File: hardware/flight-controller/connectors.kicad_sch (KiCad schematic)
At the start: 44 parts, among them J10 Conn_01x03, J11 IDC-10, J3 Conn_01x03, J4 IDC-10, J5 Conn_01x03, J6 Conn_01x03, J7 IDC-10, J8 Conn_01x03, J9 XT-30

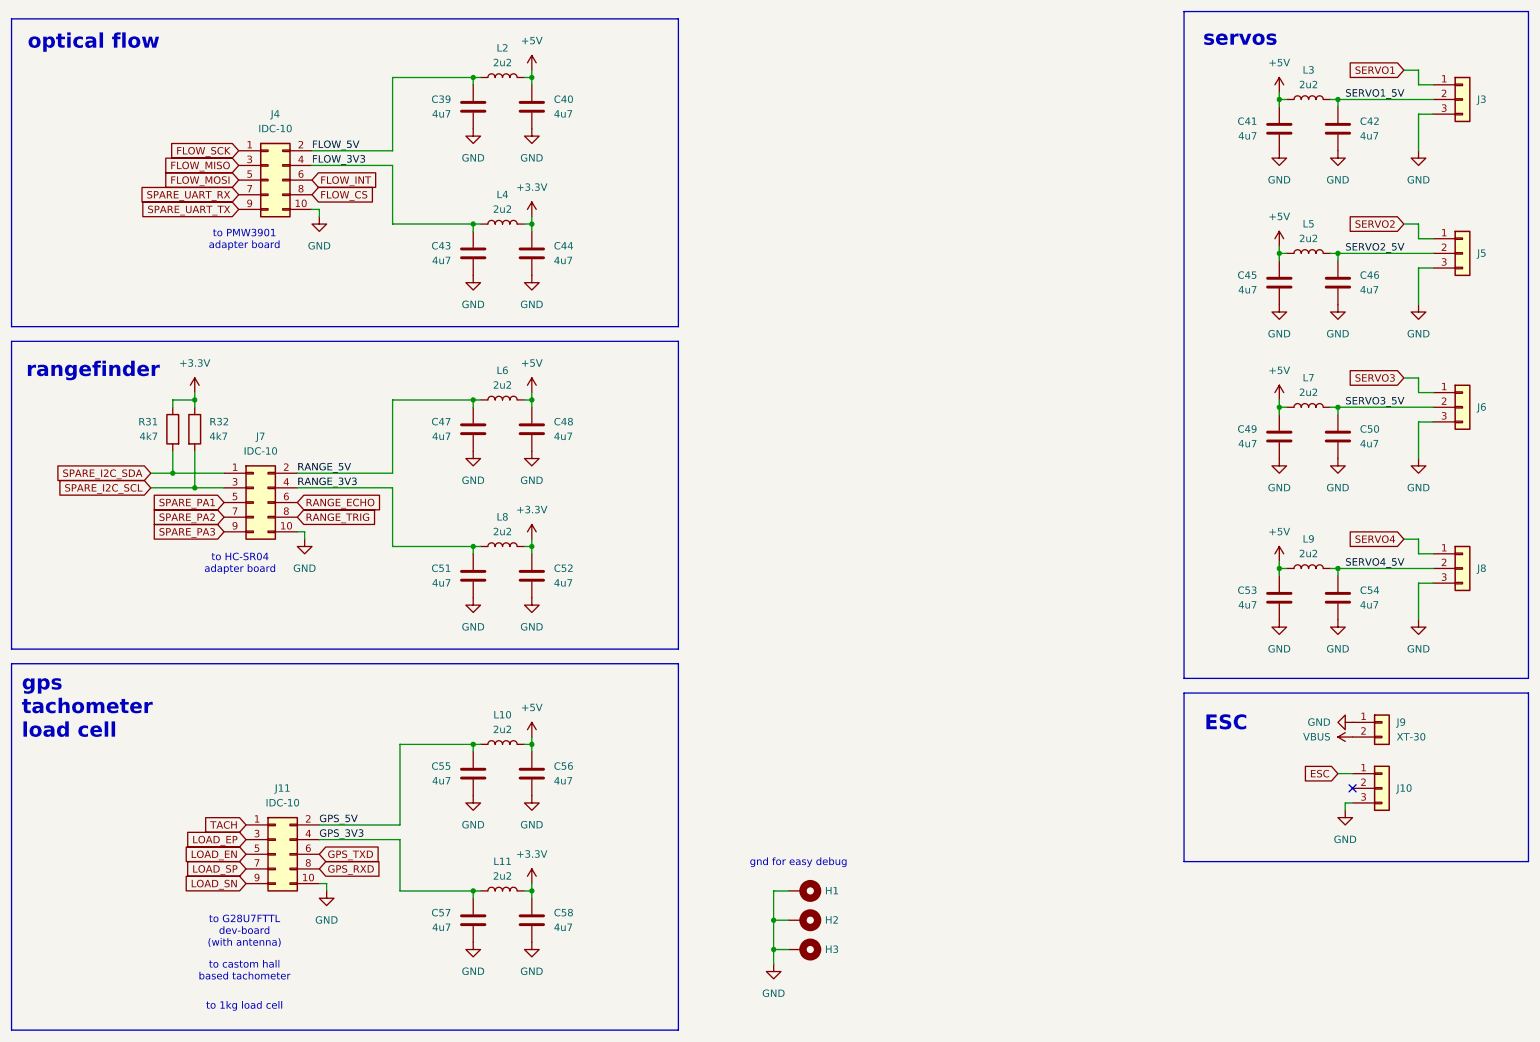
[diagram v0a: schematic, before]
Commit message: clean footprints
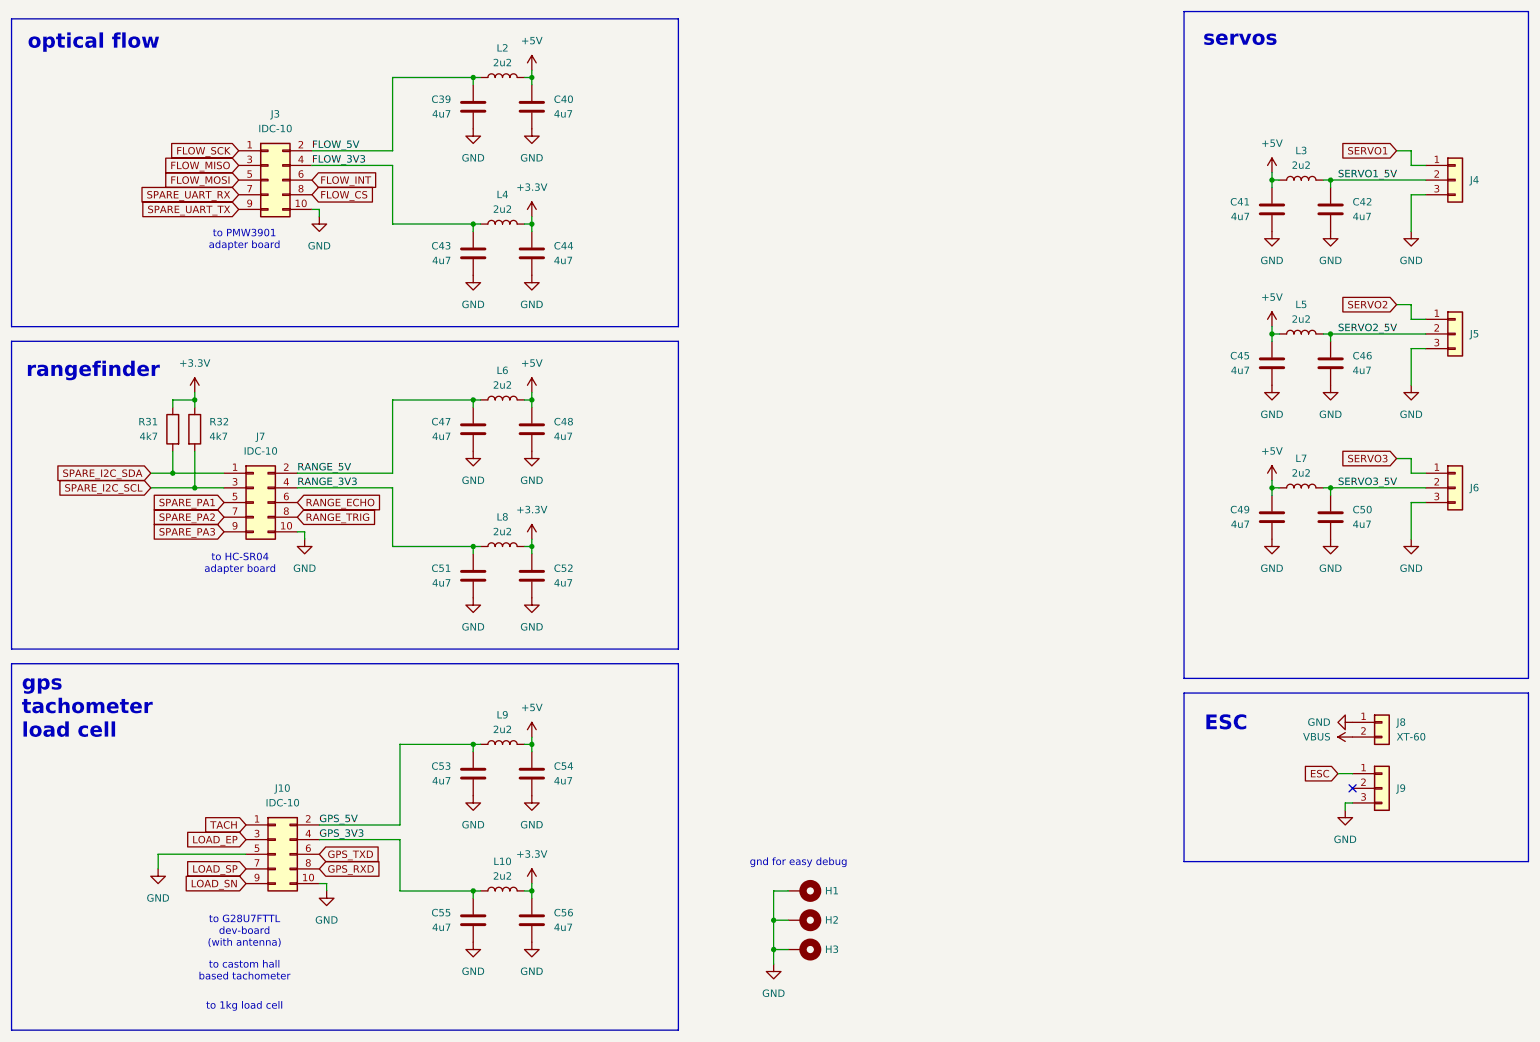
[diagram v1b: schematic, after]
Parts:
- removed C53, C54: 4u7, symbol Device:C
- removed J8: Conn_01x03, Connector_PinHeader_2.54mm:PinHeader_1x03_P2.54mm_Vertical, symbol Connector_Generic:Conn_01x03
- removed L9: 2u2, symbol Device:L
- J10: renamed from J11; footprint Connector_IDC:IDC-Header_2x05_P2.54mm_Horizontal -> goose:IDC-10-horizontal
- J3: renamed from J4; footprint Connector_IDC:IDC-Header_2x05_P2.54mm_Horizontal -> goose:IDC-10-horizontal
- J4: renamed from J3; footprint Connector_PinHeader_2.54mm:PinHeader_1x03_P2.54mm_Vertical -> goose:header_1x3
- J5, J6: footprint Connector_PinHeader_2.54mm:PinHeader_1x03_P2.54mm_Vertical -> goose:header_1x3
- J7: footprint Connector_IDC:IDC-Header_2x05_P2.54mm_Horizontal -> goose:IDC-10-horizontal
- J8: renamed from J9; value XT-30 -> XT-60; footprint Connector_AMASS:AMASS_XT30PW-F_1x02_P2.50mm_Horizontal -> goose:XT60PW-F
- J9: renamed from J10; footprint Connector_PinHeader_2.54mm:PinHeader_1x03_P2.54mm_Vertical -> goose:header_1x3
- renumbered C55 to C53, C56 to C54, C57 to C55, C58 to C56, L11 to L10, L10 to L9
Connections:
- net LOAD_EN is gone; now on net GND: J10.5 (Pin_5)
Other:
- moved on the sheet: C41, C42, C45, C46, C49, C50, J4, J5, J6, L3, L5, L7

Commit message: PI LC filters values
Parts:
- C39, C40, C41, C42, C43, C44, C45, C46, C47, C48, C49, C50, C51, C52, C53, C54, C55, C56: value 4u7 -> 10u; footprint (none) -> Capacitor_SMD:C_0603_1608Metric
- L10, L2, L3, L4, L5, L6, L7, L8, L9: footprint (none) -> Inductor_SMD:L_0603_1608Metric
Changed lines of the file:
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@@
 			)
 		)
-		(property "Footprint" ""
+		(property "Footprint" "Inductor_SMD:L_0603_1608Metric"
 			(at 242.57 97.79 0)
 			(effects
@@
 			)
 		)
-		(property "Value" "4u7"
+		(property "Value" "10u"
 			(at 251.46 50.7999 0)
 			(effects
@@
 			)
 		)
-		(property "Footprint" ""
+		(property "Footprint" "Capacitor_SMD:C_0603_1608Metric"
 			(at 248.6152 53.34 0)
 			(effects
@@
 			)
 		)
-		(property "Footprint" ""
+		(property "Footprint" "Inductor_SMD:L_0603_1608Metric"
 			(at 104.14 52.07 0)
 			(effects
@@
 		(lib_id "Device:C")
 		(at 99.06 147.32 0)
-		(mirror y)
 		(unit 1)
 		(exclude_from_sim no)
@@
 		(on_board yes)
 		(dnp no)
-		(fields_autoplaced yes)
 		(property "Reference" "C53"
 			(at 95.25 146.0499 0)
@@
 					(size 1.27 1.27)
 				)
-				(justify left)
+				(justify right)
 			)
 		)
-		(property "Value" "4u7"
+		(property "Value" "10u"
 			(at 95.25 148.5899 0)
 			(effects
@@
 					(size 1.27 1.27)
 				)
-				(justify left)
+				(justify right)
 			)
 		)
-		(property "Footprint" ""
-			(at 98.0948 151.13 0)
+		(property "Footprint" "Capacitor_SMD:C_0603_1608Metric"
+			(at 100.0252 151.13 0)
 			(effects
 				(font
@@
 			)
 		)
-		(property "Value" "4u7"
+		(property "Value" "10u"
 			(at 113.03 173.9899 0)
 			(effects
@@
 			)
 		)
-		(property "Footprint" ""
+		(property "Footprint" "Capacitor_SMD:C_0603_1608Metric"
 			(at 110.1852 176.53 0)
 			(effects
@@
 			)
 		)
-		(property "Value" "4u7"
+		(property "Value" "10u"
 			(at 113.03 88.8999 0)
 			(effects
@@
 			)
 		)
-		(property "Footprint" ""
+		(property "Footprint" "Capacitor_SMD:C_0603_1608Metric"
 			(at 110.1852 91.44 0)
 			(effects
@@
 			)
 		)
-		(property "Footprint" ""
+		(property "Footprint" "Inductor_SMD:L_0603_1608Metric"
 			(at 104.14 26.67 0)
 			(effects
@@
 			)
 		)
-		(property "Value" "4u7"
+		(property "Value" "10u"
 			(at 113.03 114.2999 0)
 			(effects
@@
 			)
 		)
-		(property "Footprint" ""
+		(property "Footprint" "Capacitor_SMD:C_0603_1608Metric"
 			(at 110.1852 116.84 0)
 			(effects
@@
 			)
 		)
-		(property "Value" "4u7"
+		(property "Value" "10u"
 			(at 251.46 77.4699 0)
 			(effects
@@
 			)
 		)
-		(property "Footprint" ""
+		(property "Footprint" "Capacitor_SMD:C_0603_1608Metric"
 			(at 248.6152 80.01 0)
 			(effects
@@
 		(lib_id "Device:C")
 		(at 99.06 31.75 0)
-		(mirror y)
 		(unit 1)
 		(exclude_from_sim no)
@@
 		(on_board yes)
 		(dnp no)
-		(fields_autoplaced yes)
 		(property "Reference" "C39"
 			(at 95.25 30.4799 0)
@@
 					(size 1.27 1.27)
 				)
-				(justify left)
+				(justify right)
 			)
 		)
-		(property "Value" "4u7"
+		(property "Value" "10u"
 			(at 95.25 33.0199 0)
 			(effects
@@
 					(size 1.27 1.27)
 				)
-				(justify left)
+				(justify right)
 			)
 		)
-		(property "Footprint" ""
-			(at 98.0948 35.56 0)
+		(property "Footprint" "Capacitor_SMD:C_0603_1608Metric"
+			(at 100.0252 35.56 0)
 			(effects
 				(font
@@
 			)
 		)
-		(property "Value" "4u7"
+		(property "Value" "10u"
 			(at 233.68 50.7999 0)
 			(effects
@@
 			)
 		)
-		(property "Footprint" ""
+		(property "Footprint" "Capacitor_SMD:C_0603_1608Metric"
 			(at 236.5248 53.34 0)
 			(effects
@@
 			)
 		)
-		(property "Value" "4u7"
+		(property "Value" "10u"
 			(at 233.68 77.4699 0)
 			(effects
@@
 			)
 		)
-		(property "Footprint" ""
+		(property "Footprint" "Capacitor_SMD:C_0603_1608Metric"
 			(at 236.5248 80.01 0)
 			(effects
@@
 			)
 		)
-		(property "Value" "4u7"
+		(property "Value" "10u"
 			(at 95.25 173.9899 0)
 			(effects
@@
 			)
 		)
-		(property "Footprint" ""
+		(property "Footprint" "Capacitor_SMD:C_0603_1608Metric"
 			(at 98.0948 176.53 0)
 			(effects
@@
 		(lib_id "Device:C")
 		(at 99.06 57.15 0)
-		(mirror y)
 		(unit 1)
 		(exclude_from_sim no)
@@
 		(on_board yes)
 		(dnp no)
-		(fields_autoplaced yes)
 		(property "Reference" "C43"
 			(at 95.25 55.8799 0)
@@
 					(size 1.27 1.27)
 				)
-				(justify left)
+				(justify right)
 			)
 		)
-		(property "Value" "4u7"
+		(property "Value" "10u"
 			(at 95.25 58.4199 0)
 			(effects
@@
 					(size 1.27 1.27)
 				)
-				(justify left)
+				(justify right)
 			)
 		)
-		(property "Footprint" ""
-			(at 98.0948 60.96 0)
+		(property "Footprint" "Capacitor_SMD:C_0603_1608Metric"
+			(at 100.0252 60.96 0)
 			(effects
 				(font
@@
 			)
 		)
-		(property "Value" "4u7"
+		(property "Value" "10u"
 			(at 113.03 148.5899 0)
 			(effects
@@
 			)
 		)
-		(property "Footprint" ""
+		(property "Footprint" "Capacitor_SMD:C_0603_1608Metric"
 			(at 110.1852 151.13 0)
 			(effects
@@
 		(lib_id "Device:C")
 		(at 99.06 113.03 0)
-		(mirror y)
 		(unit 1)
 		(exclude_from_sim no)
@@
 		(on_board yes)
 		(dnp no)
-		(fields_autoplaced yes)
 		(property "Reference" "C51"
 			(at 95.25 111.7599 0)
@@
 					(size 1.27 1.27)
 				)
-				(justify left)
+				(justify right)
 			)
 		)
-		(property "Value" "4u7"
+		(property "Value" "10u"
 			(at 95.25 114.2999 0)
 			(effects
@@
 					(size 1.27 1.27)
 				)
-				(justify left)
+				(justify right)
 			)
 		)
-		(property "Footprint" ""
-			(at 98.0948 116.84 0)
+		(property "Footprint" "Capacitor_SMD:C_0603_1608Metric"
+			(at 100.0252 116.84 0)
 			(effects
 				(font
@@
 			)
 		)
-		(property "Footprint" ""
+		(property "Footprint" "Inductor_SMD:L_0603_1608Metric"
 			(at 104.14 82.55 0)
 			(effects
@@
 			)
 		)
-		(property "Value" "4u7"
+		(property "Value" "10u"
 			(at 251.46 104.1399 0)
 			(effects
@@
 			)
 		)
-		(property "Footprint" ""
+		(property "Footprint" "Capacitor_SMD:C_0603_1608Metric"
 			(at 248.6152 106.68 0)
 			(effects
@@
 			)
 		)
-		(property "Footprint" ""
+		(property "Footprint" "Inductor_SMD:L_0603_1608Metric"
 			(at 104.14 142.24 0)
 			(effects
@@
 			)
 		)
-		(property "Footprint" ""
+		(property "Footprint" "Inductor_SMD:L_0603_1608Metric"
 			(at 104.14 107.95 0)
 			(effects
@@
 			)
 		)
-		(property "Footprint" ""
+		(property "Footprint" "Inductor_SMD:L_0603_1608Metric"
 			(at 242.57 71.12 0)
 			(effects
@@
 			)
 		)
-		(property "Footprint" ""
+		(property "Footprint" "Inductor_SMD:L_0603_1608Metric"
 			(at 242.57 44.45 0)
 			(effects
@@
 			)
 		)
-		(property "Footprint" ""
+		(property "Footprint" "Inductor_SMD:L_0603_1608Metric"
 			(at 104.14 167.64 0)
 			(effects
@@
 			)
 		)
-		(property "Value" "4u7"
+		(property "Value" "10u"
 			(at 113.03 33.0199 0)
 			(effects
@@
 			)
 		)
-		(property "Footprint" ""
+		(property "Footprint" "Capacitor_SMD:C_0603_1608Metric"
 			(at 110.1852 35.56 0)
 			(effects
@@
 		(lib_id "Device:C")
 		(at 99.06 87.63 0)
-		(mirror y)
 		(unit 1)
 		(exclude_from_sim no)
@@
 		(on_board yes)
 		(dnp no)
-		(fields_autoplaced yes)
 		(property "Reference" "C47"
 			(at 95.25 86.3599 0)
@@
 					(size 1.27 1.27)
 				)
-				(justify left)
+				(justify right)
 			)
 		)
-		(property "Value" "4u7"
+		(property "Value" "10u"
 			(at 95.25 88.8999 0)
 			(effects
@@
 					(size 1.27 1.27)
 				)
-				(justify left)
+				(justify right)
 			)
 		)
-		(property "Footprint" ""
-			(at 98.0948 91.44 0)
+		(property "Footprint" "Capacitor_SMD:C_0603_1608Metric"
+			(at 100.0252 91.44 0)
 			(effects
 				(font
@@
 			)
 		)
-		(property "Value" "4u7"
+		(property "Value" "10u"
 			(at 233.68 104.1399 0)
 			(effects
@@
 			)
 		)
-		(property "Footprint" ""
+		(property "Footprint" "Capacitor_SMD:C_0603_1608Metric"
 			(at 236.5248 106.68 0)
 			(effects
@@
 			)
 		)
-		(property "Value" "4u7"
+		(property "Value" "10u"
 			(at 113.03 58.4199 0)
 			(effects
@@
 			)
 		)
-		(property "Footprint" ""
+		(property "Footprint" "Capacitor_SMD:C_0603_1608Metric"
 			(at 110.1852 60.96 0)
 			(effects

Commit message: clean models
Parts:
- L10, L2, L3, L4, L5, L6, L7, L8, L9: value 2u2 -> 2.2u/1A
- renumbered C39 to C40, C40 to C41, C41 to C42, C42 to C43, C43 to C44, C44 to C45, C45 to C46, C46 to C47, C47 to C48, C48 to C49, C49 to C50, C50 to C51, C51 to C52, C52 to C53, C53 to C54, C54 to C55, C55 to C56, C56 to C57, R31 to R30, R32 to R31
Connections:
- net GPS_3V3 renamed GPS_TACHO_LOAD_3V3
- net GPS_5V renamed GPS_TACHO_LOAD_5V
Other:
- note added: "GND for easy prope reference"
- note removed: "gnd for easy debug"
- moved on the sheet: J10

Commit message: Mouser
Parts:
- removed L10, L2, L3, L4, L5, L6, L7, L8, L9: 2.2u/1A, Inductor_SMD:L_0603_1608Metric, symbol Device:L
- added C40, C45, C46, C51, C52, C57, C58, C61, C64: 100n, Capacitor_SMD:C_0603_1608Metric, symbol Device:C
- R30, R31: value 4k7 -> 4.7k
- renumbered C40 to C42, C42 to C43, C43 to C44, C44 to C47, C45 to C48, C46 to C49, C47 to C50, C48 to C53, C49 to C54, C50 to C55, C51 to C56, C52 to C59, C53 to C60, C54 to C62, C55 to C63, C56 to C65, C57 to C66
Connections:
- net FLOW_3V3 is gone; now on net +3.3V: C47.1, J3.4 (Pin_4)
- net FLOW_5V is gone; now on net +5V: C42.1, J3.2 (Pin_2)
- net GPS_TACHO_LOAD_3V3 is gone; now on net +3.3V: C65.1, J10.4 (Pin_4)
- net GPS_TACHO_LOAD_5V is gone; now on net +5V: C62.1, J10.2 (Pin_2)
- net RANGE_3V3 is gone; now on net +3.3V: C59.1, J7.4 (Pin_4)
- net RANGE_5V is gone; now on net +5V: C53.1, J7.2 (Pin_2)
- net SERVO1_5V is gone; now on net +5V: C44.1, J4.2 (Pin_2)
- net SERVO2_5V is gone; now on net +5V: C50.1, J5.2 (Pin_2)
- net SERVO3_5V is gone; now on net +5V: C56.1, J6.2 (Pin_2)
- net +3.3V: now also C46.1, C58.1, C64.1
- net +5V: now also C40.1, C45.1, C51.1, C52.1, C57.1, C61.1
- net GND: now also C40.2, C45.2, C46.2, C51.2, C52.2, C57.2, C58.2, C61.2, C64.2
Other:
- moved on the sheet: C42, C43, C44, C47, C48, C49, C50, C53, C54, C55, C56, C59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

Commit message: routing: all signals routed
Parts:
- renumbered R31 to R30, R30 to R31
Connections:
- net FLOW_CS: now also J3.9 (Pin_9); no longer J3.8 (Pin_8)
- net FLOW_MISO: now also J3.8 (Pin_8); no longer J3.3 (Pin_3)
- net FLOW_SCK: now also J3.7 (Pin_7); no longer J3.1 (Pin_1)
- net GND: now also J10.6 (Pin_6); no longer J10.5 (Pin_5)
- net GPS_TXD: now also J10.9 (Pin_9); no longer J10.6 (Pin_6)
- net LOAD_SN: now also J10.5 (Pin_5); no longer J10.9 (Pin_9)
- net RANGE_ECHO: now also J7.3 (Pin_3); no longer J7.6 (Pin_6)
- net RANGE_TRIG: now also J7.1 (Pin_1); no longer J7.8 (Pin_8)
- net SPARE_I2C_SCL: now also J7.8 (Pin_8); no longer J7.3 (Pin_3)
- net SPARE_I2C_SDA: now also J7.6 (Pin_6); no longer J7.1 (Pin_1)
- net SPARE_UART_RX: now also J3.3 (Pin_3); no longer J3.7 (Pin_7)
- net SPARE_UART_TX: now also J3.1 (Pin_1); no longer J3.9 (Pin_9)
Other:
- moved on the sheet: J7, R30, R31

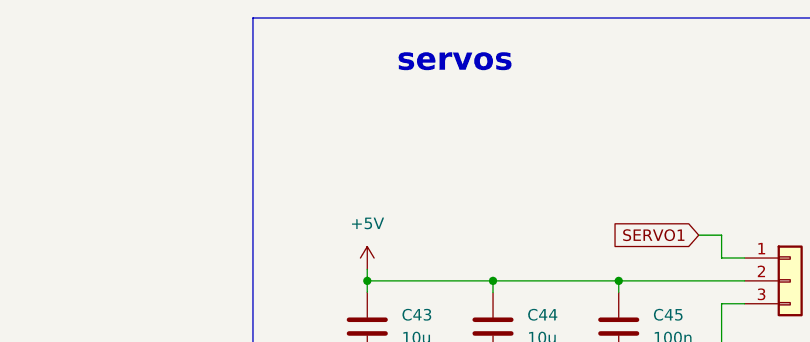
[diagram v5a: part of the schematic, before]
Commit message: fix IMU interrupt
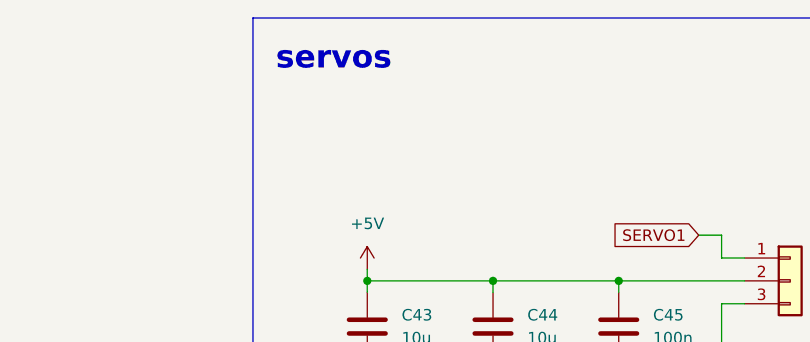
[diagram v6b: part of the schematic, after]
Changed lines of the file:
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@@
 	(title_block
 		(title "UAV TVC Goose Flight Controller")
-		(date "2024-08-04")
+		(date "2024-08-05")
 		(rev "V2.1")
 		(comment 4 "Author: Eryk Możdżeń")
@@
 	(text "servos"
 		(exclude_from_sim no)
-		(at 225.552 20.066 0)
+		(at 212.09 19.812 0)
 		(effects
 			(font
